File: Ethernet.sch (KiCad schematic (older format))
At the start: 16 parts, among them J1 Wuerth_7499010121A, U3 DP83848C

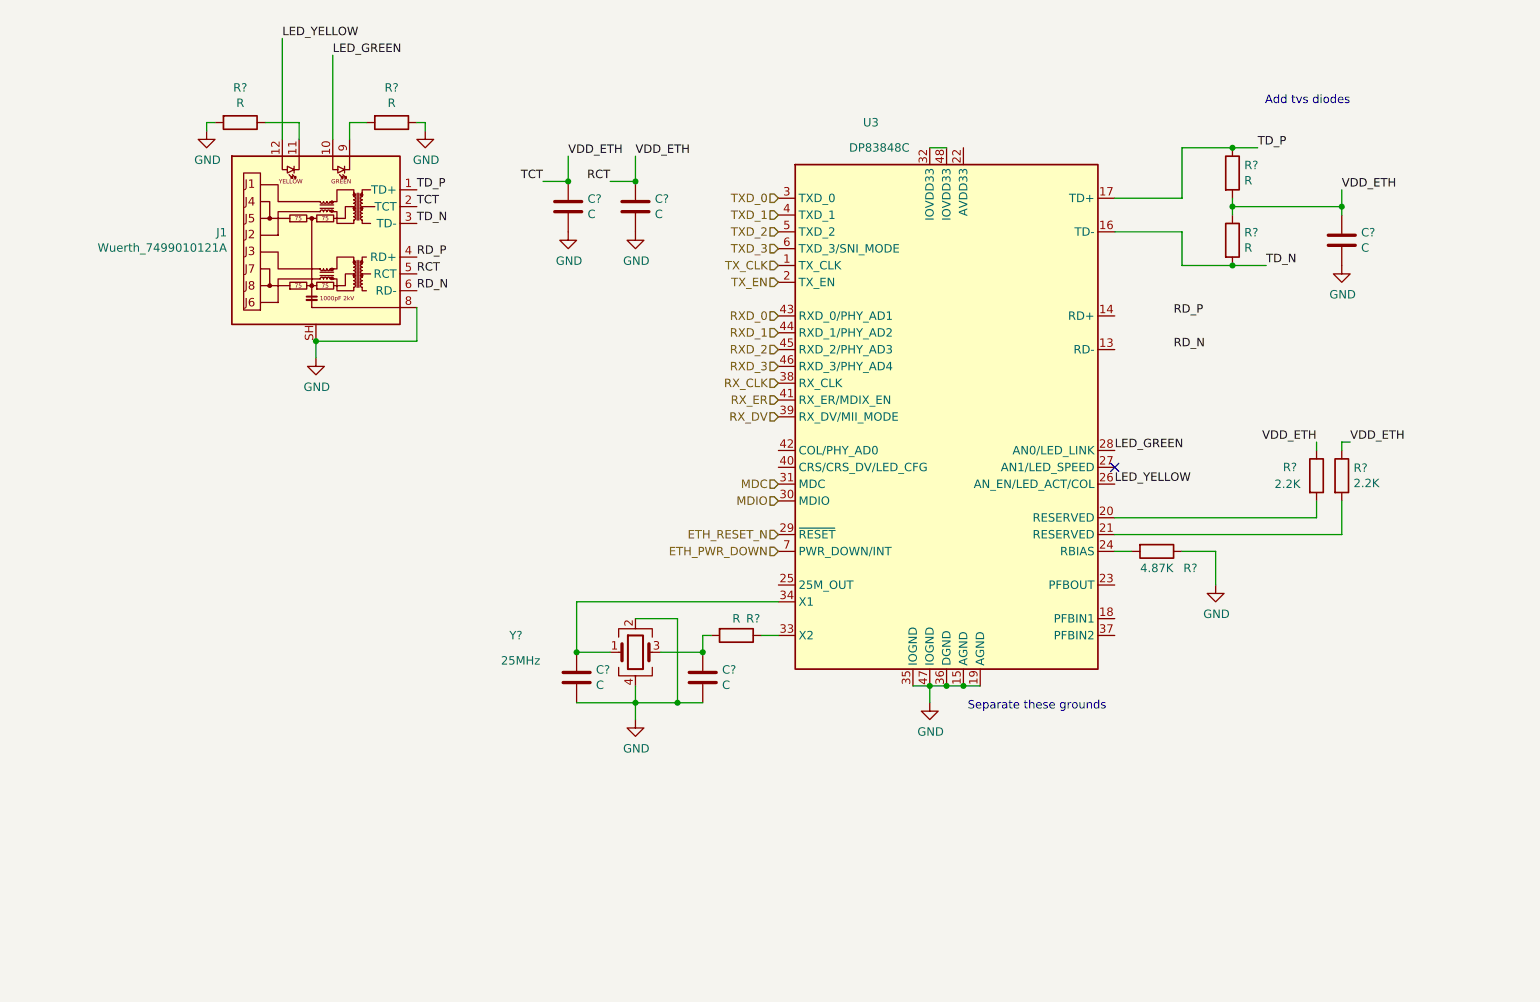
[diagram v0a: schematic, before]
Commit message: Add bulk labels for RAM and ethernet
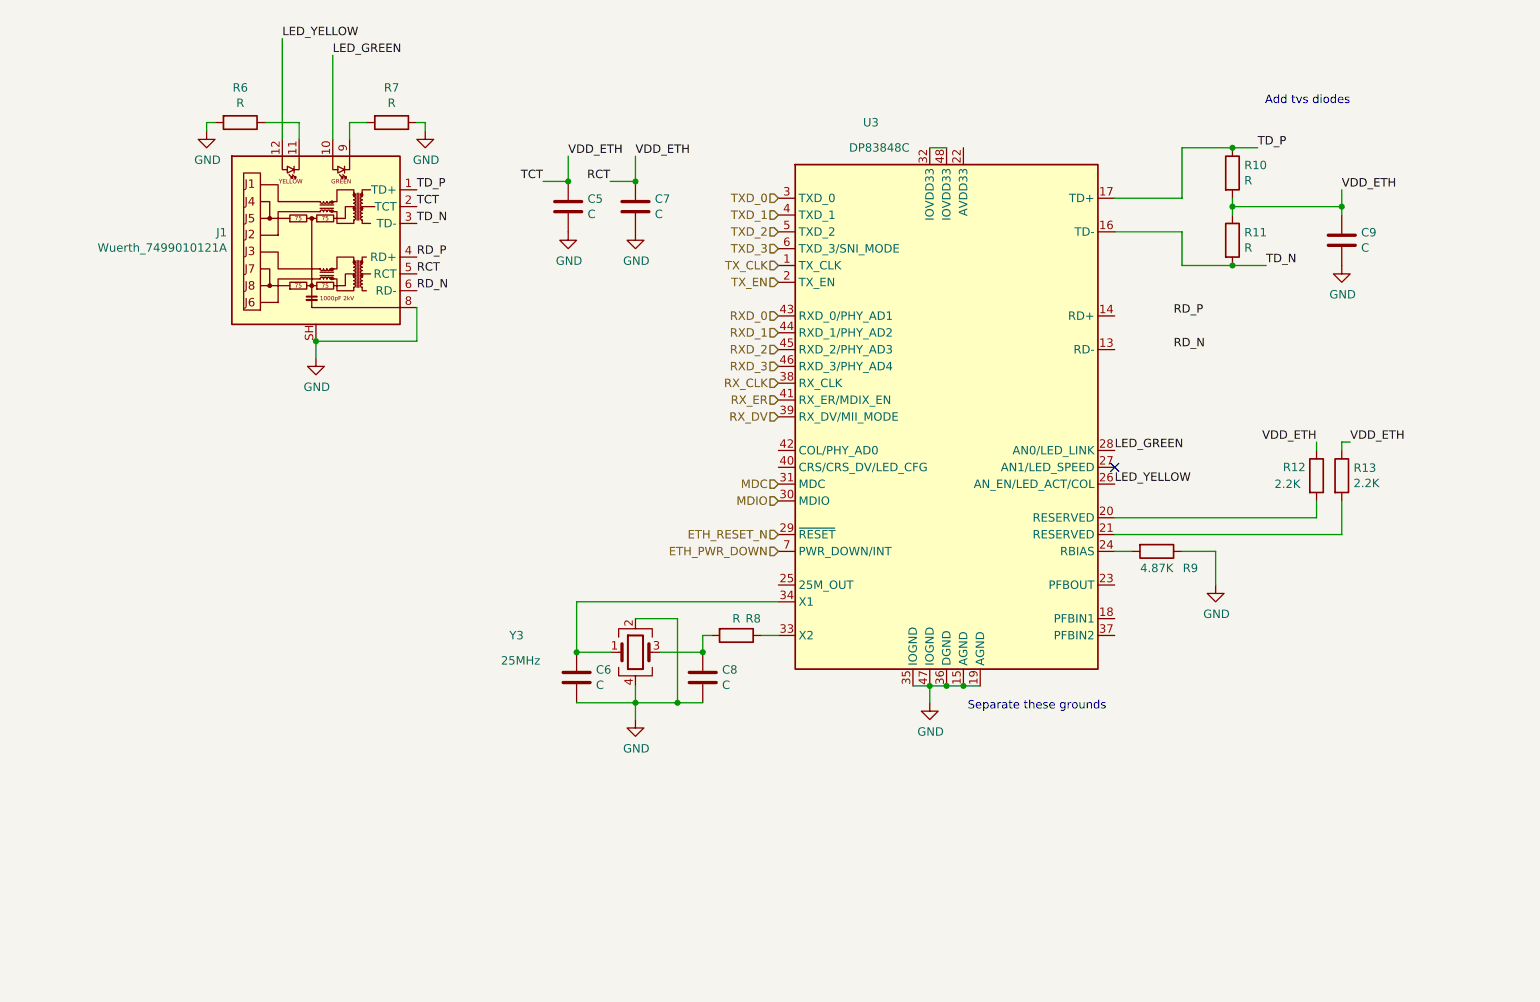
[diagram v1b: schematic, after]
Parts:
- C5, C6, C7, C8, C9: renamed from C?; footprint (none) -> Capacitor_SMD:C_0603_1608Metric
- R10, R11, R12, R13, R6, R7, R8, R9: renamed from R?; footprint (none) -> Resistor_SMD:R_0603_1608Metric
- Y3: renamed from Y?; footprint (none) -> Crystal:Crystal_SMD_2520-4Pin_2.5x2.0mm
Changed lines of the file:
@@
 TCT
 $Comp
-L Device:Crystal_GND24 Y?
+L Device:Crystal_GND24 Y3
 U 1 1 603F557C
 P 5000 4650
-F 0 "Y?" H 4250 4750 50  0000 L CNN
+F 0 "Y3" H 4250 4750 50  0000 L CNN
 F 1 "25MHz" H 4200 4600 50  0000 L CNN
-F 2 "" H 5000 4650 50  0001 C CNN
+F 2 "Crystal:Crystal_SMD_2520-4Pin_2.5x2.0mm" H 5000 4650 50  0001 C CNN
 F 3 "~" H 5000 4650 50  0001 C CNN
 	1    5000 4650
@@
 	3200 1600 3200 1100
 $Comp
-L Device:R R?
+L Device:R R9
 U 1 1 60426F43
 P 8100 4050
-F 0 "R?" V 8200 4250 50  0000 C CNN
+F 0 "R9" V 8200 4250 50  0000 C CNN
 F 1 "4.87K" V 8200 4050 50  0000 C CNN
-F 2 "" V 8030 4050 50  0001 C CNN
+F 2 "Resistor_SMD:R_0603_1608Metric" V 8030 4050 50  0001 C CNN
 F 3 "~" H 8100 4050 50  0001 C CNN
 	1    8100 4050
@@
 	9050 3850 9050 3750
 $Comp
-L Device:R R?
+L Device:R R12
 U 1 1 60431953
 P 9050 3600
-F 0 "R?" H 8850 3650 50  0000 L CNN
+F 0 "R12" H 8850 3650 50  0000 L CNN
 F 1 "2.2K" H 8800 3550 50  0000 L CNN
-F 2 "" V 8980 3600 50  0001 C CNN
+F 2 "Resistor_SMD:R_0603_1608Metric" V 8980 3600 50  0001 C CNN
 F 3 "~" H 9050 3600 50  0001 C CNN
 	1    9050 3600
@@
 $EndComp
 $Comp
-L Device:R R?
+L Device:R R13
 U 1 1 60432320
 P 9200 3600
-F 0 "R?" H 9270 3646 50  0000 L CNN
+F 0 "R13" H 9270 3646 50  0000 L CNN
 F 1 "2.2K" H 9270 3555 50  0000 L CNN
-F 2 "" V 9130 3600 50  0001 C CNN
+F 2 "Resistor_SMD:R_0603_1608Metric" V 9130 3600 50  0001 C CNN
 F 3 "~" H 9200 3600 50  0001 C CNN
 	1    9200 3600
@@
 ETH_PWR_DOWN
 $Comp
-L Device:R R?
+L Device:R R6
 U 1 1 60447515
 P 2650 1500
-F 0 "R?" V 2443 1500 50  0000 C CNN
+F 0 "R6" V 2443 1500 50  0000 C CNN
 F 1 "R" V 2534 1500 50  0000 C CNN
-F 2 "" V 2580 1500 50  0001 C CNN
+F 2 "Resistor_SMD:R_0603_1608Metric" V 2580 1500 50  0001 C CNN
 F 3 "~" H 2650 1500 50  0001 C CNN
 	1    2650 1500
@@
 $EndComp
 $Comp
-L Device:R R?
+L Device:R R7
 U 1 1 60448348
 P 3550 1500
-F 0 "R?" V 3343 1500 50  0000 C CNN
+F 0 "R7" V 3343 1500 50  0000 C CNN
 F 1 "R" V 3434 1500 50  0000 C CNN
-F 2 "" V 3480 1500 50  0001 C CNN
+F 2 "Resistor_SMD:R_0603_1608Metric" V 3480 1500 50  0001 C CNN
 F 3 "~" H 3550 1500 50  0001 C CNN
 	1    3550 1500
@@
 	5000 4950 5000 4850
 $Comp
-L power:GND #PWR?
+L power:GND #PWR017
 U 1 1 61275BF5
 P 5000 5050
-F 0 "#PWR?" H 5000 4800 50  0001 C CNN
+F 0 "#PWR017" H 5000 4800 50  0001 C CNN
 F 1 "GND" H 5005 4877 50  0000 C CNN
 F 2 "" H 5000 5050 50  0001 C CNN
@@
 $EndComp
 $Comp
-L Device:C C?
+L Device:C C8
 U 1 1 6127676A
 P 5400 4800
-F 0 "C?" H 5515 4846 50  0000 L CNN
+F 0 "C8" H 5515 4846 50  0000 L CNN
 F 1 "C" H 5515 4755 50  0000 L CNN
-F 2 "" H 5438 4650 50  0001 C CNN
+F 2 "Capacitor_SMD:C_0603_1608Metric" H 5438 4650 50  0001 C CNN
 F 3 "~" H 5400 4800 50  0001 C CNN
 	1    5400 4800
@@
 Connection ~ 5250 4950
 $Comp
-L Device:C C?
+L Device:C C6
 U 1 1 6127941C
 P 4650 4800
-F 0 "C?" H 4765 4846 50  0000 L CNN
+F 0 "C6" H 4765 4846 50  0000 L CNN
 F 1 "C" H 4765 4755 50  0000 L CNN
-F 2 "" H 4688 4650 50  0001 C CNN
+F 2 "Capacitor_SMD:C_0603_1608Metric" H 4688 4650 50  0001 C CNN
 F 3 "~" H 4650 4800 50  0001 C CNN
 	1    4650 4800
@@
 	6750 4850 6750 4950
 $Comp
-L power:GND #PWR?
+L power:GND #PWR018
 U 1 1 6127D98C
 P 6750 4950
-F 0 "#PWR?" H 6750 4700 50  0001 C CNN
+F 0 "#PWR018" H 6750 4700 50  0001 C CNN
 F 1 "GND" H 6755 4777 50  0000 C CNN
 F 2 "" H 6750 4950 50  0001 C CNN
@@
 	8250 4050 8450 4050
 $Comp
-L power:GND #PWR?
+L power:GND #PWR019
 U 1 1 61281321
 P 8450 4250
-F 0 "#PWR?" H 8450 4000 50  0001 C CNN
+F 0 "#PWR019" H 8450 4000 50  0001 C CNN
 F 1 "GND" H 8455 4077 50  0000 C CNN
 F 2 "" H 8450 4250 50  0001 C CNN
@@
 	8450 4050 8450 4250
 $Comp
-L power:GND #PWR?
+L power:GND #PWR012
 U 1 1 61288464
 P 2450 1550
-F 0 "#PWR?" H 2450 1300 50  0001 C CNN
+F 0 "#PWR012" H 2450 1300 50  0001 C CNN
 F 1 "GND" H 2455 1377 50  0000 C CNN
 F 2 "" H 2450 1550 50  0001 C CNN
@@
 	2450 1500 2500 1500
 $Comp
-L power:GND #PWR?
+L power:GND #PWR014
 U 1 1 6128C03D
 P 3750 1550
-F 0 "#PWR?" H 3750 1300 50  0001 C CNN
+F 0 "#PWR014" H 3750 1300 50  0001 C CNN
 F 1 "GND" H 3755 1377 50  0000 C CNN
 F 2 "" H 3750 1550 50  0001 C CNN
@@
 	4450 1850 4600 1850
 $Comp
-L Device:C C?
+L Device:C C5
 U 1 1 6129C44C
 P 4600 2000
-F 0 "C?" H 4715 2046 50  0000 L CNN
+F 0 "C5" H 4715 2046 50  0000 L CNN
 F 1 "C" H 4715 1955 50  0000 L CNN
-F 2 "" H 4638 1850 50  0001 C CNN
+F 2 "Capacitor_SMD:C_0603_1608Metric" H 4638 1850 50  0001 C CNN
 F 3 "~" H 4600 2000 50  0001 C CNN
 	1    4600 2000
@@
 $EndComp
 $Comp
-L Device:C C?
+L Device:C C7
 U 1 1 6129CAC4
 P 5000 2000
-F 0 "C?" H 5115 2046 50  0000 L CNN
+F 0 "C7" H 5115 2046 50  0000 L CNN
 F 1 "C" H 5115 1955 50  0000 L CNN
-F 2 "" H 5038 1850 50  0001 C CNN
+F 2 "Capacitor_SMD:C_0603_1608Metric" H 5038 1850 50  0001 C CNN
 F 3 "~" H 5000 2000 50  0001 C CNN
 	1    5000 2000
@@
 	4850 1850 5000 1850
 $Comp
-L power:GND #PWR?
+L power:GND #PWR015
 U 1 1 6129E14A
 P 4600 2150
-F 0 "#PWR?" H 4600 1900 50  0001 C CNN
+F 0 "#PWR015" H 4600 1900 50  0001 C CNN
 F 1 "GND" H 4605 1977 50  0000 C CNN
 F 2 "" H 4600 2150 50  0001 C CNN
@@
 $EndComp
 $Comp
-L power:GND #PWR?
+L power:GND #PWR016
 U 1 1 6129E969
 P 5000 2150
-F 0 "#PWR?" H 5000 1900 50  0001 C CNN
+F 0 "#PWR016" H 5000 1900 50  0001 C CNN
 F 1 "GND" H 5005 1977 50  0000 C CNN
 F 2 "" H 5000 2150 50  0001 C CNN
@@
 Connection ~ 5000 1850
 $Comp
-L Device:R R?
+L Device:R R8
 U 1 1 612B0691
 P 5600 4550
-F 0 "R?" V 5500 4650 50  0000 C CNN
+F 0 "R8" V 5500 4650 50  0000 C CNN
 F 1 "R" V 5500 4550 50  0000 C CNN
-F 2 "" V 5530 4550 50  0001 C CNN
+F 2 "Resistor_SMD:R_0603_1608Metric" V 5530 4550 50  0001 C CNN
 F 3 "~" H 5600 4550 50  0001 C CNN
 	1    5600 4550
@@
 	5750 4550 5850 4550
 $Comp
-L Device:R R?
+L Device:R R10
 U 1 1 612C9A25
 P 8550 1800
-F 0 "R?" H 8620 1846 50  0000 L CNN
+F 0 "R10" H 8620 1846 50  0000 L CNN
 F 1 "R" H 8620 1755 50  0000 L CNN
-F 2 "" V 8480 1800 50  0001 C CNN
+F 2 "Resistor_SMD:R_0603_1608Metric" V 8480 1800 50  0001 C CNN
 F 3 "~" H 8550 1800 50  0001 C CNN
 	1    8550 1800
@@
 $EndComp
 $Comp
-L Device:R R?
+L Device:R R11
 U 1 1 612CA17F
 P 8550 2200
-F 0 "R?" H 8620 2246 50  0000 L CNN
+F 0 "R11" H 8620 2246 50  0000 L CNN
 F 1 "R" H 8620 2155 50  0000 L CNN
-F 2 "" V 8480 2200 50  0001 C CNN
+F 2 "Resistor_SMD:R_0603_1608Metric" V 8480 2200 50  0001 C CNN
 F 3 "~" H 8550 2200 50  0001 C CNN
 	1    8550 2200
@@
 $EndComp
 $Comp
-L Device:C C?
+L Device:C C9
 U 1 1 612CDAE6
 P 9200 2200
-F 0 "C?" H 9315 2246 50  0000 L CNN
+F 0 "C9" H 9315 2246 50  0000 L CNN
 F 1 "C" H 9315 2155 50  0000 L CNN
-F 2 "" H 9238 2050 50  0001 C CNN
+F 2 "Capacitor_SMD:C_0603_1608Metric" H 9238 2050 50  0001 C CNN
 F 3 "~" H 9200 2200 50  0001 C CNN
 	1    9200 2200
@@
 Connection ~ 9200 2000
 $Comp
-L power:GND #PWR?
+L power:GND #PWR020
 U 1 1 612D8764
 P 9200 2350
-F 0 "#PWR?" H 9200 2100 50  0001 C CNN
+F 0 "#PWR020" H 9200 2100 50  0001 C CNN
 F 1 "GND" H 9205 2177 50  0000 C CNN
 F 2 "" H 9200 2350 50  0001 C CNN
@@
 VDD_ETH
 $Comp
-L power:GND #PWR?
+L power:GND #PWR013
 U 1 1 612EDD5D
 P 3100 2900
-F 0 "#PWR?" H 3100 2650 50  0001 C CNN
+F 0 "#PWR013" H 3100 2650 50  0001 C CNN
 F 1 "GND" H 3105 2727 50  0000 C CNN
 F 2 "" H 3100 2900 50  0001 C CNN

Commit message: Complete ethernet and PMIC circuitry
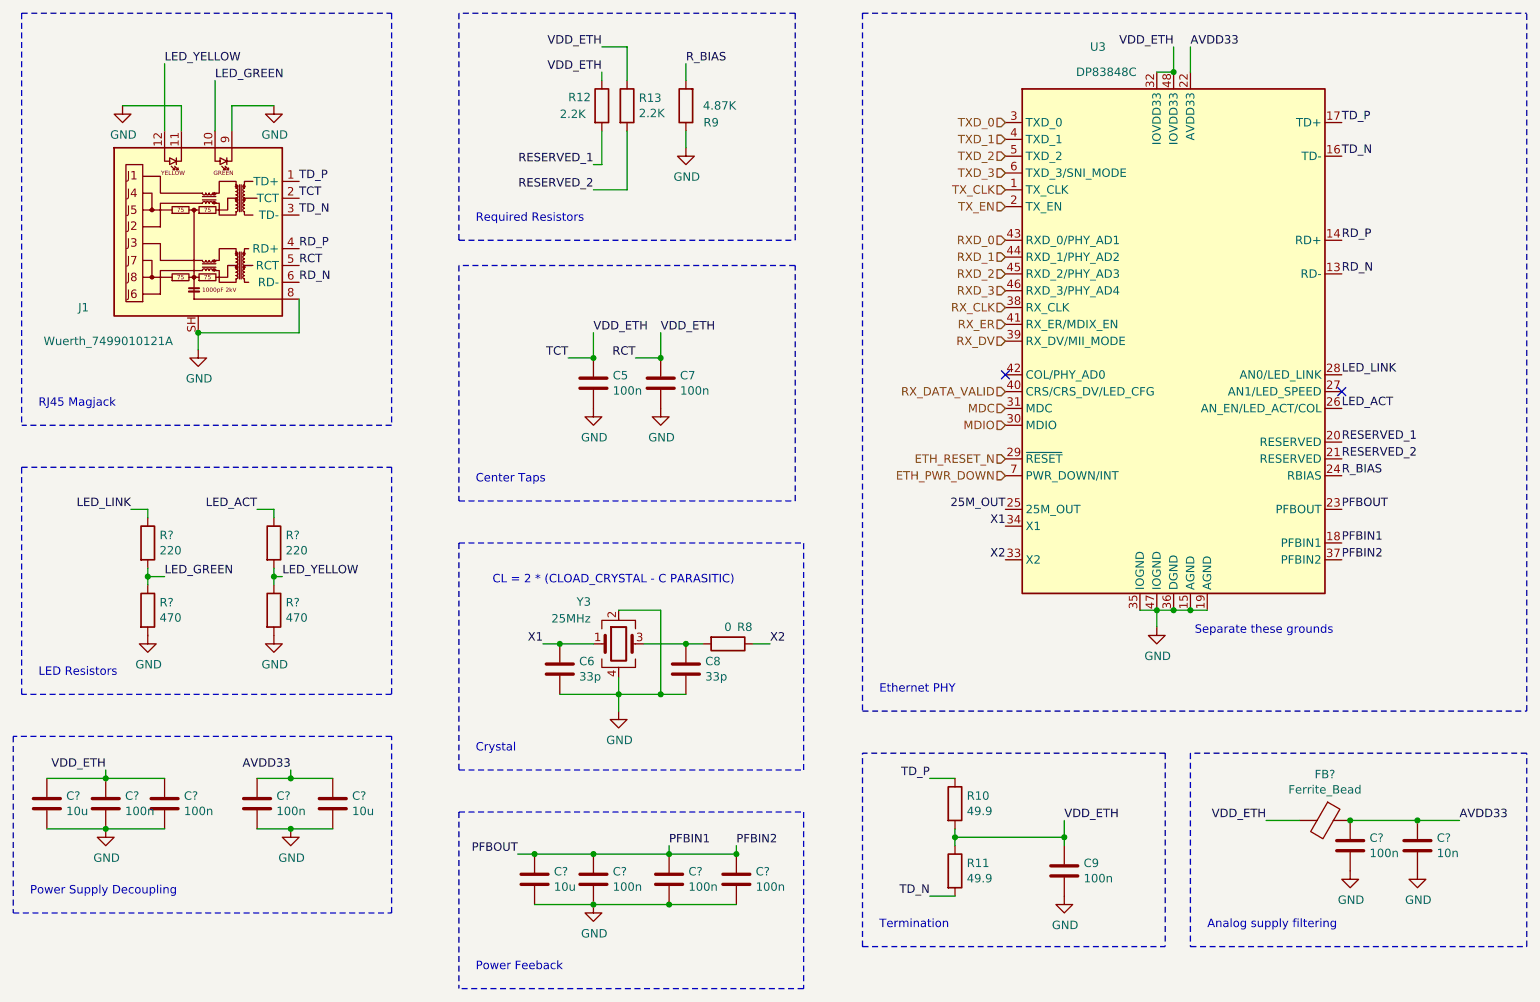
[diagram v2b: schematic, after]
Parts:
- removed R6, R7: R, Resistor_SMD:R_0603_1608Metric, symbol Device:R
- added C? (x3): 10u, symbol Device:C
- added C? (x7): 100n, symbol Device:C
- added C?: 10n, symbol Device:C
- added FB?: Ferrite_Bead, symbol Device:Ferrite_Bead
- added R? (x2): 220, symbol Device:R
- added R? (x2): 470, symbol Device:R
- C5, C7, C9: value C -> 100n
- C6, C8: value C -> 33p
- R10, R11: value R -> 49.9
- R8: value R -> 0
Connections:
- net GND: now also J1.11, J1.9, C?.2, C?.2, C?.2, C?.2, C?.2, C?.2, C?.2, C?.2, C?.2, C?.2, C?.2, R?.2, R?.2
- net LED_GREEN: now also R?.1, R?.2; no longer U3.28 (AN0/LED_LINK)
- net LED_YELLOW: now also R?.1, R?.2; no longer U3.26 (AN_EN/LED_ACT/COL)
- net RCT: now also U3.32 (IOVDD33), U3.48 (IOVDD33), C?.1, C?.1, C?.1, FB?.2
- net RD_N: now also U3.13 (RD-)
- net RD_P: now also U3.14 (RD+)
- net PFBIN1: now reaches U3.18 (PFBIN1)
- net PFBIN1: now also U3.23 (PFBOUT), U3.37 (PFBIN2), C?.1, C?.1, C?.1, C?.1
- net RESERVED_1: now reaches R12.2, U3.20 (RESERVED)
- net RESERVED_2: now reaches R13.2, U3.21 (RESERVED)
- net AVDD33: now reaches U3.22 (AVDD33)
- net AVDD33: now also C?.1, C?.1, C?.1, C?.1, FB?.1
- net R_BIAS: now reaches R9.2, U3.24 (RBIAS)
- net 25M_OUT: now reaches U3.25 (25M_OUT)
- net X2: now reaches R8.1, U3.33 (X2)
- net X1: now reaches C6.1, U3.34 (X1), Y3.1
- net RX_DATA_VALID: now reaches U3.40 (CRS/CRS_DV/LED_CFG)
- new net LED_ACT: R?.1, U3.26 (AN_EN/LED_ACT/COL)
- new net LED_LINK: R?.1, U3.28 (AN0/LED_LINK)
- no-connect marks 1 -> 2
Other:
- note added: "Analog supply filtering"
- note added: "CL = 2 * (CLOAD_CRYSTAL - C PARASITIC)"
- note added: "Center Taps"
- note added: "Crystal\n"
- note added: "Ethernet PHY"
- note added: "LED Resistors"
- note added: "Power Feeback\n"
- note added: "Power Supply Decoupling\n"
- note added: "RJ45 Magjack\n"
- note added: "Required Resistors\n"
- note added: "Termination\n"
- note removed: "Add tvs diodes\n"
- moved on the sheet: C5, C6, C7, C8, C9, J1, R10, R11, R12, R13, R8, R9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
